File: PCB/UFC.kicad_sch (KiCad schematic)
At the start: 61 parts, among them M1 Fan_3pin, M2 Fan_3pin, M3 Fan_3pin, M4 Fan_3pin, M5 Fan_3pin, M6 Fan_3pin, M7 Fan_3pin, M8 Fan_3pin, SW1 PWM 12:5, U1 Pico

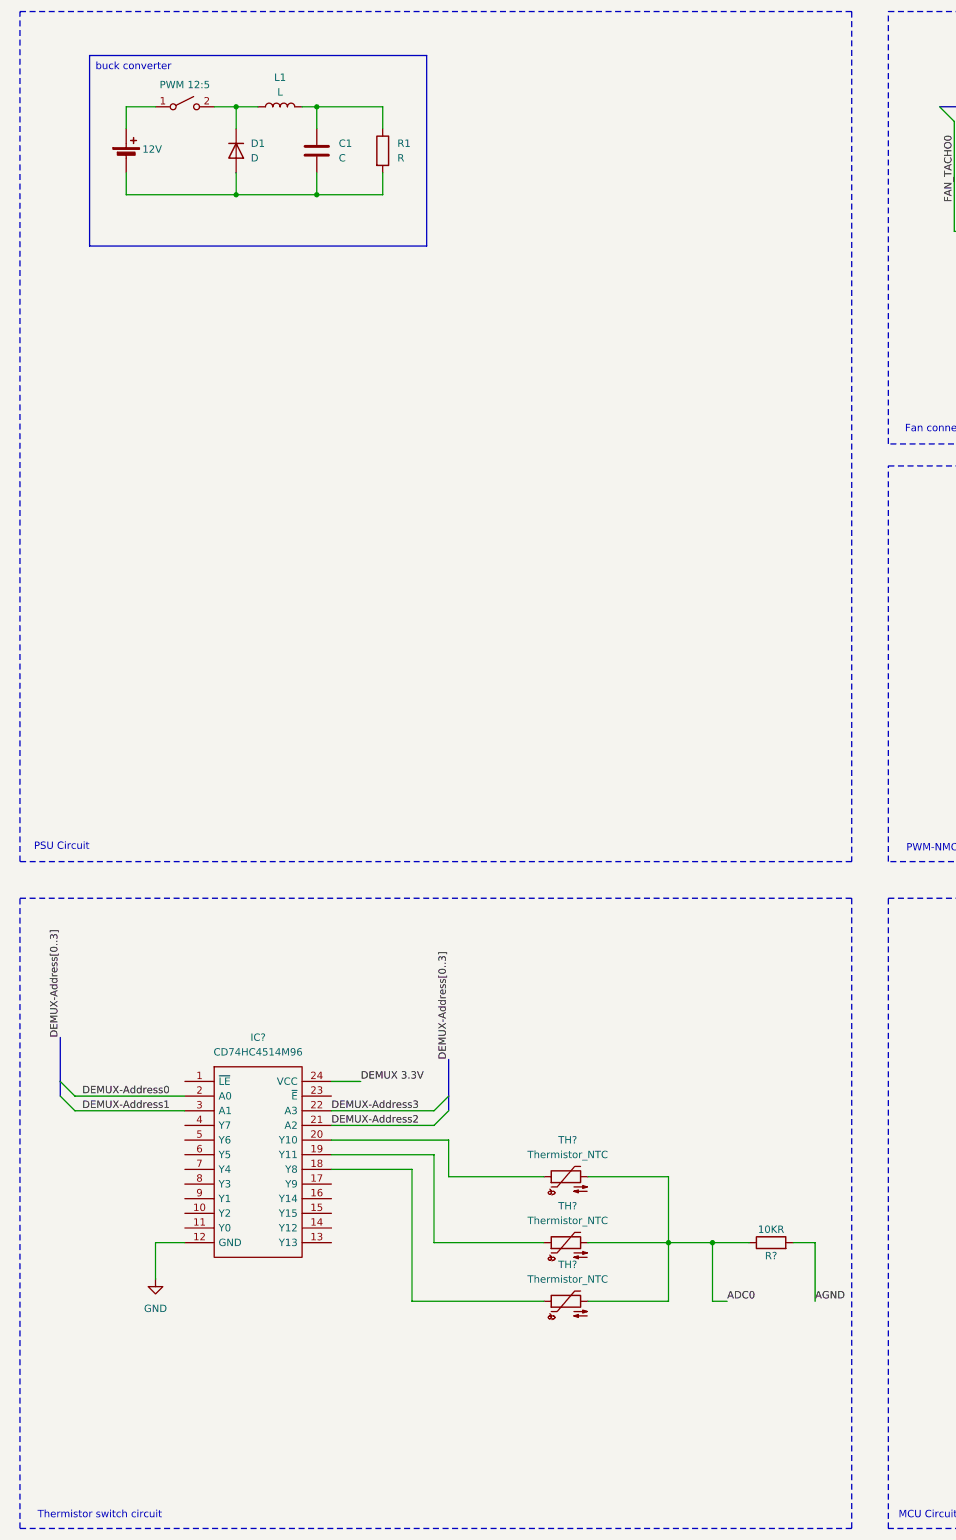
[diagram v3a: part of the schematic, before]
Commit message: Thermistor update
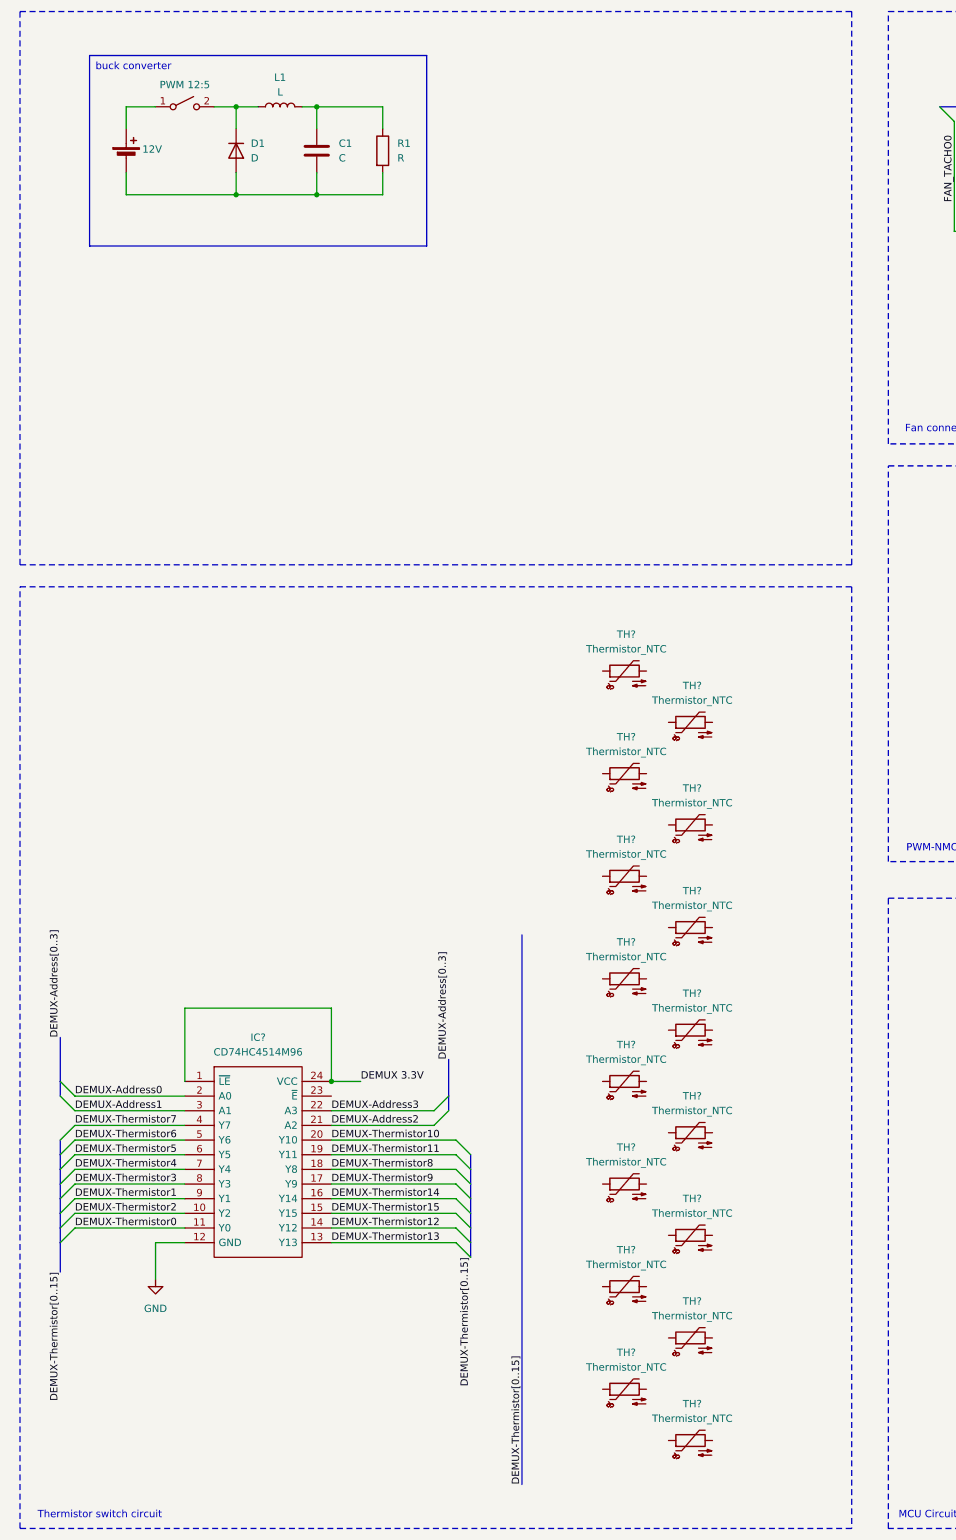
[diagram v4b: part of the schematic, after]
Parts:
- removed R?: 10KR, symbol Device:R
- removed TH? (x3): Thermistor_NTC, symbol Device:Thermistor_NTC
- added TH? (x16): Thermistor_NTC, symbol Device:Thermistor_NTC
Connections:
- net DEMUX 3.3V: now also IC?.1 (~{LE})
- net DEMUX-Thermistor2: now reaches IC?.10 (Y2)
- net DEMUX-Thermistor0: now reaches IC?.11 (Y0)
- net DEMUX-Thermistor13: now reaches IC?.13 (Y13)
- net DEMUX-Thermistor12: now reaches IC?.14 (Y12)
- net DEMUX-Thermistor15: now reaches IC?.15 (Y15)
- net DEMUX-Thermistor14: now reaches IC?.16 (Y14)
- net DEMUX-Thermistor9: now reaches IC?.17 (Y9)
- net DEMUX-Thermistor8: now reaches IC?.18 (Y8)
- net DEMUX-Thermistor11: now reaches IC?.19 (Y11)
- net DEMUX-Thermistor10: now reaches IC?.20 (Y10)
- net DEMUX-Thermistor7: now reaches IC?.4 (Y7)
- net DEMUX-Thermistor6: now reaches IC?.5 (Y6)
- net DEMUX-Thermistor5: now reaches IC?.6 (Y5)
- net DEMUX-Thermistor4: now reaches IC?.7 (Y4)
- net DEMUX-Thermistor3: now reaches IC?.8 (Y3)
- net DEMUX-Thermistor1: now reaches IC?.9 (Y1)
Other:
- note removed: "PSU Circuit"

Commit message: update
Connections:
- net DEMUX-Thermistor0: now also TH?.1
- net DEMUX-Thermistor1: now also TH?.1
- net DEMUX-Thermistor10: now also TH?.1
- net DEMUX-Thermistor11: now also TH?.1
- net DEMUX-Thermistor12: now also TH?.1
- net DEMUX-Thermistor13: now also TH?.1
- net DEMUX-Thermistor14: now also TH?.1
- net DEMUX-Thermistor15: now also TH?.1
- net DEMUX-Thermistor2: now also TH?.1
- net DEMUX-Thermistor3: now also TH?.1
- net DEMUX-Thermistor4: now also TH?.1
- net DEMUX-Thermistor5: now also TH?.1
- net DEMUX-Thermistor6: now also TH?.1
- net DEMUX-Thermistor7: now also TH?.1
- net DEMUX-Thermistor8: now also TH?.1
- net DEMUX-Thermistor9: now also TH?.1
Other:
- moved on the sheet: IC?, TH?

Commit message: Finished demux prototype
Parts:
- added R?: 10kR, symbol Device:R
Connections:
- net ADC0: now also TH?.2, TH?.2, TH?.2, TH?.2, TH?.2, TH?.2, TH?.2, TH?.2, TH?.2, TH?.2, TH?.2, TH?.2, TH?.2, TH?.2, TH?.2, TH?.2, R?.2
- net AGND: now also R?.1
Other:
- moved on the sheet: TH?

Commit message: Relay polishing
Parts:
- removed K?: G5Q-1, Relay_THT:Relay_SPDT_Omron-G5Q-1, symbol Relay:G5Q-1
- added F?: Main 12V Fuse, symbol Device:Fuse
- added K?: EP1-3N1S, EP13N1S, symbol UFC_Lib:EP1-3N1S
- D?: value Emergency Mode LED -> Failure LED
- renumbered BT1 to BT?, C1 to C?, D1 to D?, L1 to L?, M4 to M?, M7 to M?, M8 to M?, M6 to M?, M2 to M?, M3 to M?, M1 to M?, M5 to M?, R1 to R?, SW to SW?, SW1 to SW?, U1 to U?
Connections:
- net +12V: now also K?.3 (COIL_2)
- net DEMUX 3.3V: no longer U?.35 (ADC_VREF)
- net GND: now also F?.2
- net Relay_closed: now also K?.5 (NC)
- net Relay_open: now also K?.4 (NO)
- net at D?.2 (A), Q?.1 (D): now also K?.2 (COIL_1)
- new net: F?.1, K?.1 (COM)
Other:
- note removed: "Note: Find actual relay symbol"
- moved on the sheet: D?, Q?, R?, SW?

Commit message: tacho
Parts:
- removed BT?: 12V, symbol Device:Battery_Cell
- removed C?: C, symbol Device:C
- removed D?: D, symbol Device:D
- removed L?: L, symbol Device:L
- removed R?: R, symbol Device:R
- removed SW?: PWM 12:5, symbol Switch:SW_SPST
- added Q1, Q2, Q3, Q4, Q5, Q6, Q7, Q8: NMOS, symbol Simulation_SPICE:NMOS
- added R1, R2, R3, R4, R5, R6, R7, R8: R, symbol Device:R
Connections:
- net +5V: now also R1.1, R2.1, R3.1, R4.1, R5.1, R6.1, R7.1, R8.1
- net FAN_TACHO0: now also Q1.2 (G)
- net FAN_TACHO1: now also Q2.2 (G)
- net FAN_TACHO2: now also Q3.2 (G)
- net FAN_TACHO3: now also Q4.2 (G)
- net FAN_TACHO4: now also Q5.2 (G)
- net FAN_TACHO5: now also Q6.2 (G)
- net FAN_TACHO6: now also Q7.2 (G)
- net FAN_TACHO7: now also Q8.2 (G)
- net GND: now also Q1.3 (S), Q2.3 (S), Q3.3 (S), Q4.3 (S), Q5.3 (S), Q6.3 (S), Q7.3 (S), Q8.3 (S)
- net Tacho0: now also Q1.1 (D), R1.2
- net Tacho1: now also Q2.1 (D), R2.2
- net Tacho2: now also Q3.1 (D), R3.2
- net Tacho3: now also Q4.1 (D), R4.2
- net Tacho4: now also Q5.1 (D), R5.2
- net Tacho6: now also Q7.1 (D), R7.2
- net Tacho7: now also Q8.1 (D), R8.2
- new net Tacho5: Q6.1 (D), R6.2
